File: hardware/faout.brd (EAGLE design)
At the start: 100 x 80 mm, 150 parts, among them IC2 MT48LC8M16A2, Q1 12MHz, Q4 ASFL, U1 93LC46BT-I/OT, U10 REF102AU, U11 OPA4277UA, U12 DAC8812, U13 OPA4277UA, U14 REF102AU, U15 DAC8812, U16 OPA4277UA, U17 OPA2277UA/2K5E4, U2 REF102AU, U3 L7812ACV, U4 L7912ACV, U5 LM3671MF-3.3, U6 LM3671MF-1.2, U7 M25PE16SO8N, U8 6SLX9TQG144, U9 DAC8812

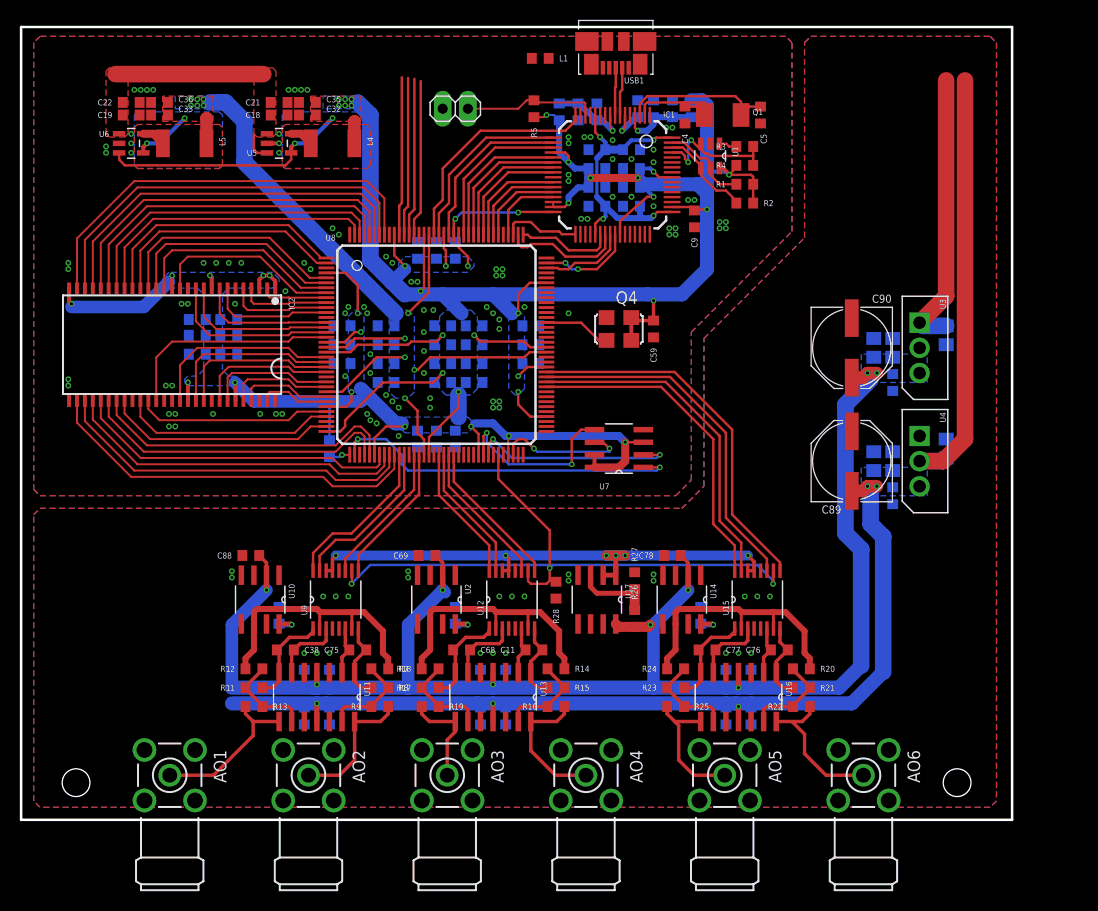
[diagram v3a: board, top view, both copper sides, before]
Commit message: WIP: Compress FAOUT-6 layout to 7cm, use space for connectors.
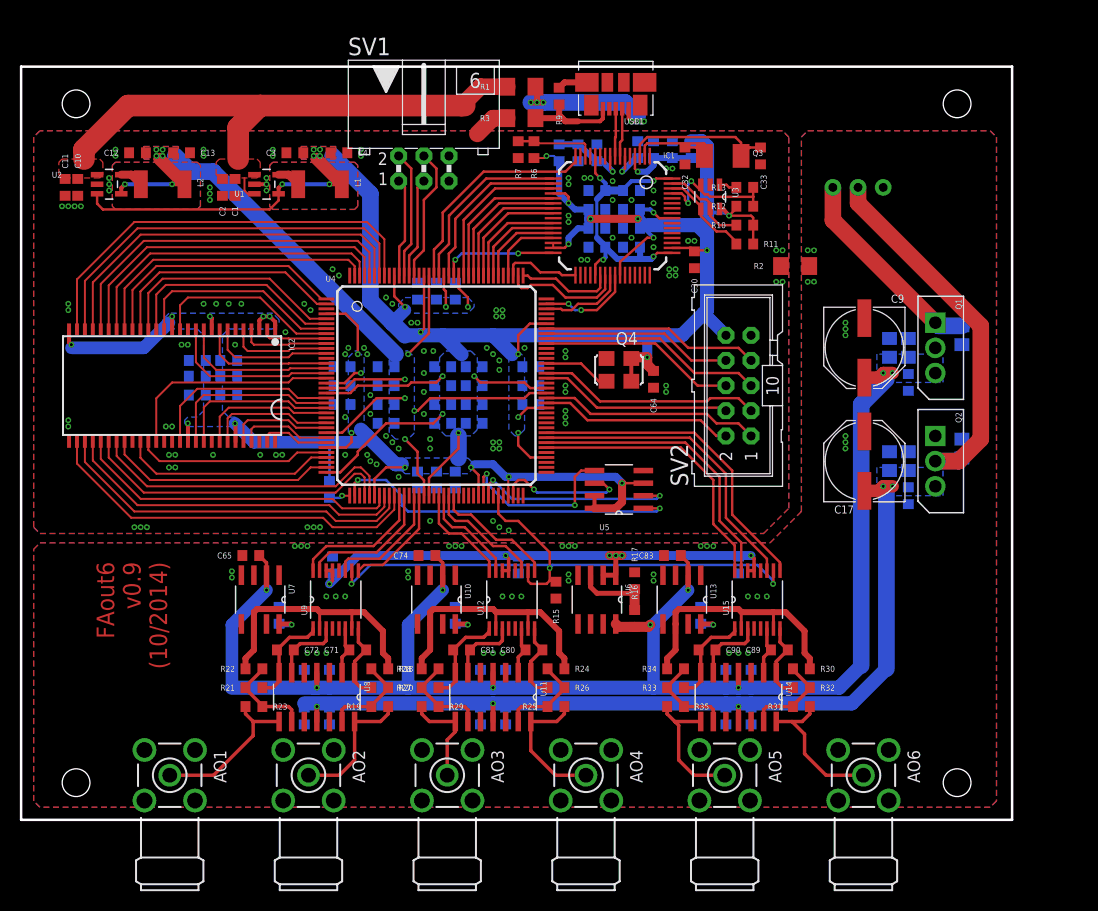
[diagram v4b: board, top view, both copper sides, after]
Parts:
- removed L3: (no value), faout:R0603
- removed L4, L5: 2.2uH, rcl:L5038P
- removed U16: OPA4277UA, faout:SOIC127P600X175-14N
- removed U17: OPA2277UA/2K5E4, faout:SOIC127P600X175-8N
- removed USB_RST: (no value), pinhead:1X02
- added C86: 1uF, faout:R0603
- added C87, C91: 100nF, faout:R0603
- added P1: TE_CONN_MTE_HEADER3R, faout:TE_CONN_MTE_HEADER3_R
- added Q2: L7912ACV, faout:TO254P450X1020X1935-3P
- added Q3: 12MHz, faout:TXC_QUARTZ_7A
- added R29, R30, R31, R34, R35: 10k, faout:R0603
- added R32, R33: 5k, faout:R0603
- added SV1: (no value), con-ml:ML6L
- added SV2: (no value), con-ml:ML10
- C1, C12, C13, C2: value 10uF -> 4.7uF; device faout:R0805 -> faout:R0603
- C11: value 20pF -> 4.7uF
- C14: value 10uF -> 100nF; device faout:R0805 -> faout:R0603
- C16, C7: value 100nF -> 10uF; device faout:R0603 -> faout:R0805
- C17, C9: value 100nF -> 100uF; device faout:R0603 -> rcl:PANASONIC_E
- C18, C8: value 4.7uF -> 10uF; device faout:R0603 -> faout:R0805
- C20: value 100nF -> 4.7uF
- C21, C22: value 4.7uF -> 100nF
- C29, C30: value 470nF -> 100nF
- C3: value 3.3uF -> 4.7uF
- C31: value 4.7uF -> 3.3uF
- C32, C33: value 4.7uF -> 18pF
- C34, C35, C43, C44, C46, C49, C56: value 4.7uF -> 470nF
- C37, C59: value 10nF -> 4.7uF
- C38: value 20pF -> 10nF
- C4: value 18pF -> 4.7uF
- C42, C48, C54, C60, C62: value 470nF -> 4.7uF
- C5: value 18pF -> 10uF; device faout:R0603 -> faout:R0805
- C64: value 4.7uF -> 10nF
- C68, C75, C76, C77: value 20pF -> 1uF
- C69, C70, C73, C78, C79, C88: value 1uF -> 100nF
- C71, C72, C80, C81: value 100nF -> 20pF
- C83: value 100nF -> 1uF
- C89, C90: value 100uF -> 20pF; device rcl:PANASONIC_E -> faout:R0603
- L1, L2: value (none) -> 2.2uH; device faout:R0603 -> rcl:L5038P
- Q1: value 12MHz -> L7812ACV; device faout:TXC_QUARTZ_7A -> faout:TO254P450X1020X1935-3P
- R1, R2: value 10k -> ferrite; device faout:R0603 -> faout:R1206
- R10: value 4.7k -> 10k
- R11, R15, R23: value 5k -> 10k
- R13: value 10k -> 2.2k
- R14: value 10k -> 4.7k
- R16: value 10k -> 13.181k
- R20: value 10k -> 5k
- R26: value 13.181k -> 5k
- R3: value 2.2k -> ferrite; device faout:R0603 -> faout:R1206
- R4, R5: value 10k -> ferrite
- R6: value 12k -> 10k
- R7: value 10k -> NC
- R8: value 5k -> 12k
- R9: value 10k -> (none)
- U1: value 93LC46BT-I/OT -> LM3671MF-3.3; device faout:SOT95P280X145-6N -> faout:SOT95P284X122-5N
- U13: value OPA4277UA -> REF102AU; device faout:SOIC127P600X175-14N -> faout:SOIC127P600X175-8N
- U14: value REF102AU -> OPA4277UA; device faout:SOIC127P600X175-8N -> faout:SOIC127P600X175-14N
- U2: value REF102AU -> LM3671MF-1.2; device faout:SOIC127P600X175-8N -> faout:SOT95P284X122-5N
- U3: value L7812ACV -> 93LC46BT-I/OT; device faout:TO254P450X1020X1935-3P -> faout:SOT95P280X145-6N
- U4: value L7912ACV -> 6SLX9TQG144; device faout:TO254P450X1020X1935-3P -> faout:TQ144
- U5: value LM3671MF-3.3 -> M25PE16SO8N; device faout:SOT95P284X122-5N -> faout:SOIC127P600X175-8N
- U6: value LM3671MF-1.2 -> OPA2277UA/2K5E4; device faout:SOT95P284X122-5N -> faout:SOIC127P600X175-8N
- U7: value M25PE16SO8N -> REF102AU
- U8: value 6SLX9TQG144 -> OPA4277UA; device faout:TQ144 -> faout:SOIC127P600X175-14N
- moved C12 78.7 mm to (11.7, 67.3), flipped to the top, turned to 180 degrees
- moved C13 78.2 mm to (16.2, 67.3), flipped to the top, turned to 0 degrees
- moved C2 77.6 mm to (20.3, 63.8), flipped to the top, turned to 270 degrees
- moved C18 76.7 mm to (94.9, 37.5), flipped to the bottom, turned to 90 degrees
- moved C1 73.3 mm to (21.6, 63.8), flipped to the top
- moved R13 72.1 mm to (73.0, 63.8), turned to 180 degrees
- moved R12 68.1 mm to (73.0, 61.9)
- moved R11 66.8 mm to (73.0, 58.1), turned to 0 degrees
- moved C11 66.5 mm to (4.45, 63.8), turned to 270 degrees
- moved U6 65.8 mm to (58.1, 22.2), turned to 270 degrees
- moved R9 64.2 mm to (54.3, 73.0), turned to 270 degrees
- moved C33 60.8 mm to (74.6, 67.0), turned to 270 degrees
- moved R8 60.2 mm to (62.2, 67.6), flipped to the bottom, turned to 90 degrees
- moved R22 55.4 mm to (23.5, 15.2)
- moved R21 55.2 mm to (23.5, 13.3), turned to 180 degrees
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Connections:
- removed net N$16: L1.1, USB1.M6
- new net N$15: R9.1, USB1.M6
- new net P1_1: SV2.1, U4.88
- new net P1_2: SV2.2, U4.87
- new net P1_3: SV2.3, U4.93
- new net P1_4: SV2.4, U4.92
- new net P1_5: SV2.5, U4.100
- new net P1_6: SV2.6, U4.99
- new net P1_7: SV2.7, U4.102
- new net P1_8: SV2.8, U4.101
- net !DAC1_CS: now also U4.50; no longer U8.50
- net !DAC1_LDAC: now also U4.48; no longer U8.48
- net !DAC2_CS: now also U4.57; no longer U8.57
- net !DAC2_LDAC: now also U4.56; no longer U8.56
- net !DAC3_CS: now also U4.80; no longer U8.84
- net !DAC3_LDAC: now also U4.79; no longer U8.83
- net !DACX_RS: now also R15.1, U4.67; no longer R28.1, U8.67
- net !RAM_CAS: now also U4.5; no longer U8.5
- net !RAM_RAS: now also U4.2; no longer U8.2
- net !RAM_WE: now also U4.6; no longer U8.6
- net !USB_OE: now also U4.111; no longer U8.111
- net !USB_RD: now also U4.114; no longer U8.114
- net !USB_RESET: now also R6.1, R7.1; no longer R5.1, USB_RST.1
- net !USB_RXF: now also U4.116; no longer U8.116
- net !USB_TXE: now also U4.115; no longer U8.115
- net !USB_WR: now also U4.112; no longer U8.112
- net +15V: now also C5.1, P1.P$1, Q1.1; no longer C1.1, U3.1
- net -15V: now also C18.1, P1.P$2, Q2.2; no longer C2.1, U4.2
- net 1V2: now also C12.1, C13.1, C52.1, C53.1, C54.1, C55.1, L2.2, U2.4, U4.128, U4.19, U4.28, U4.52, U4.89; no longer C33.1, C36.1, C41.1, C43.1, C45.1, C46.1, L5.2, U6.4, U8.128, U8.19, U8.28, U8.52, U8.89
- net 1V8: now also C25.1, C31.1; no longer C20.1, C3.1
- net 3V3: now also C3.1, C36.1, C38.1, C4.1, C41.1, C43.1, C45.1, C46.1, L1.2, R11.2, R12.2, R14.2, R4.1, R5.1, R6.2, SV2.10, U1.4, U2.3, U3.6, U4.103, U4.122, U4.125, U4.129, U4.135, U4.18, U4.20, U4.31, U4.36, U4.4, U4.42, U4.53, U4.63, U4.69, U4.76, U4.86, U4.90, U5.3, U5.7, U5.8; no longer C25.1, C31.1, C32.1, C52.1, C53.1, C54.1, C55.1, C9.1, L2.1, L3.1, L4.2, R1.2, R2.2, R4.2, R5.2, U1.6, U5.4, U6.3, U7.3, U7.7, U7.8, U8.103, U8.122, U8.125, U8.129, U8.135, U8.18, U8.20, U8.31, U8.36, U8.4, U8.42, U8.53, U8.63, U8.69, U8.76, U8.86, U8.90
- net 5V0: now also C1.1, C10.1, C11.1, C2.1, R1.2, U1.1, U1.3, U2.1; no longer C18.1, C19.1, C21.1, C22.1, U5.1, U5.3, U6.1
- net A+12V: now also C65.1, C67.1, C7.1, C74.1, C76.1, C8.1, C83.1, C85.1, C87.1, C9.+, Q1.3, R16.1, U13.2, U14.4, U6.8, U7.2, U8.4; no longer C12.1, C14.1, C66.1, C71.1, C73.1, C80.1, C82.1, C84.1, C88.1, C90.+, R26.1, U13.4, U14.2, U16.4, U17.8, U2.2, U3.3
- net A+3V3: now also C73.1, C82.1, C91.1, U6.1, U6.2; no longer U17.1, U17.2
- net A-12V: now also C14.2, C16.2, C17.-, C68.2, C70.2, C77.2, C79.2, C86.2, C88.2, Q2.3, U14.11, U8.11; no longer C13.2, C67.2, C7.2, C72.2, C74.2, C81.2, C83.2, C85.2, C89.-, U13.11, U16.11, U4.3
- net AGND: now also C14.1, C16.1, C17.+, C18.2, C5.2, C67.2, C68.1, C7.2, C70.1, C74.2, C75.2, C76.2, C77.1, C79.1, C8.2, C83.2, C85.2, C86.1, C87.2, C88.1, C9.-, C91.2, P1.P$3, Q1.2, Q2.1, R15.2, R17.2, R2.1, U13.4, U14.10, U14.12, U14.3, U14.5, U6.4, U7.4, U8.10, U8.12, U8.3, U8.5; no longer C1.2, C12.2, C13.1, C14.2, C2.2, C67.1, C7.1, C70.2, C71.2, C72.1, C74.1, C79.2, C80.2, C81.1, C83.1, C85.1, C88.2, C89.+, C90.-, R27.2, R28.2, U13.10, U13.12, U13.3, U13.5, U14.4, U16.10, U16.12, U16.3, U16.5, U17.4, U2.4, U3.2, U4.1
- net CLK_IN: now also U4.95; no longer U8.95
- net DAC1_CLK: now also U4.47; no longer U8.47
- net DAC1_IOUTA: now also C72.2, U8.6; no longer C38.2, U11.6
- net DAC1_IOUTB: now also C71.2, U8.2; no longer C75.2, U11.2
- net DAC1_RFBA: now also C72.1, R21.1, U8.7; no longer C38.1, R11.1, U11.7
- net DAC1_RFBB: now also C71.1, R20.1, U8.1; no longer C75.1, R8.1, U11.1
- net DAC1_SDI: now also U4.51; no longer U8.51
- net DAC1_VOUTA: now also R23.1, U8.8; no longer R13.1, U11.8
- net DAC1_VOUTB: now also R19.1, U8.14; no longer R9.1, U11.14
- net DAC1_VREF: now also R18.2, R22.2, U7.6; no longer R12.2, R7.2, U10.6
- net DAC2_CLK: now also U4.55; no longer U8.55
- net DAC2_IOUTA: now also C81.2, U11.6; no longer C68.2, U13.6
- net DAC2_IOUTB: now also C80.2, U11.2; no longer C11.2, U13.2
- net DAC2_RFBA: now also C81.1, R27.1, U11.7; no longer C68.1, R17.1, U13.7
- net DAC2_RFBB: now also C80.1, R26.1, U11.1; no longer C11.1, R15.1, U13.1
- net DAC2_SDI: now also U4.58; no longer U8.58
- net DAC2_VOUTA: now also R29.1, U11.8; no longer R19.1, U13.8
- net DAC2_VOUTB: now also R25.1, U11.14; no longer R16.1, U13.14
- net DAC2_VREF: now also R24.2, R28.2, U10.6; no longer R14.2, R18.2, U2.6
- net DAC3_CLK: now also U4.78; no longer U8.82
- net DAC3_IOUTA: now also C90.2, U14.6; no longer C77.2, U16.6
- net DAC3_IOUTB: now also C89.2, U14.2; no longer C76.2, U16.2
- net DAC3_RFBA: now also C90.1, R33.1, U14.7; no longer C77.1, R23.1, U16.7
- net DAC3_RFBB: now also C89.1, R32.1, U14.1; no longer C76.1, R21.1, U16.1
- net DAC3_SDI: now also U4.81; no longer U8.85
- net DAC3_VOUTA: now also R35.1, U14.8; no longer R25.1, U16.8
- net DAC3_VOUTB: now also R31.1, U14.14; no longer R22.1, U16.14
- net DAC3_VREF: now also R30.2, R34.2, U13.6; no longer R20.2, R24.2, U14.6
- net EECS: now also R10.1, U3.5; no longer R1.1, U1.5
- net EEDATA: now also R12.1, R13.1, U3.3; no longer R3.1, R4.1, U1.3
- net EESK: now also R11.1, U3.4; no longer R2.1, U1.4
- net FLASH_CS: now also U4.38, U5.1; no longer U7.1, U8.38
- net FLASH_MISO: now also U4.65, U5.2; no longer U7.2, U8.65
- net FLASH_MOSI: now also U4.64, U5.5; no longer U7.5, U8.64
- net FLASH_SCK: now also U4.70, U5.6; no longer U7.6, U8.70
- net GND: now also C1.2, C11.2, C12.2, C13.2, C2.2, C38.2, R2.2, R3.2, R7.2, R8.2, SV1.5, SV1.6, SV2.9, U2.2, U3.2, U4.104, U4.105, U4.108, U4.113, U4.13, U4.130, U4.136, U4.144, U4.25, U4.3, U4.34, U4.49, U4.54, U4.59, U4.60, U4.61, U4.62, U4.66, U4.68, U4.73, U4.77, U4.82, U4.83, U4.84, U4.85, U4.91, U4.94, U4.96, U4.97, U4.98, U5.4; no longer C16.2, C17.2, C18.2, C5.2, C8.2, C9.2, L1.2, R6.2, U5.2, U6.2, U7.4, U8.108, U8.113, U8.13, U8.130, U8.136, U8.144, U8.25, U8.3, U8.49, U8.54, U8.60, U8.68, U8.73, U8.77, U8.91, U8.96, USB_RST.2
- net GPIO_0_0: now also SV1.1, U4.134; no longer U8.134
- net GPIO_0_1: now also SV1.2, U4.133; no longer U8.133
- net GPIO_0_2: now also SV1.3, U4.132; no longer U8.132
- net GPIO_0_3: now also SV1.4, U4.131; no longer U8.131
- net N$1: now also C32.1, Q3.1; no longer C4.1, Q1.1
- net N$10: now also R30.1, R31.2, R32.2, U14.13; no longer R20.1, R21.2, R22.2, U16.13
- net N$11: now also C75.1, U10.8; no longer C70.1, U2.8
- net N$12: now also C84.1, U13.8; no longer C79.1, U14.8
- net N$13: now also R16.2, R17.1, U6.3; no longer R26.2, R27.1, U17.3
- net N$14: now also R33.2, R34.1, R35.2, U14.9; no longer R23.2, R24.1, R25.2, U16.9
- net N$2: now also C33.1, Q3.2; no longer C5.1, Q1.2
- net N$20: now also R27.2, R28.1, R29.2, U11.9; no longer R17.2, R18.1, R19.2, U13.9
- net N$21: now also R24.1, R25.2, R26.2, U11.13; no longer R14.1, R15.2, R16.2, U13.13
- net N$24: now also L1.1, U1.5; no longer L4.1, U5.5
- net N$25: now also L2.1, U2.5; no longer L5.1, U6.5
- net N$4: now also C66.1, U7.8; no longer C65.1, U10.8
- net N$5: now also C19.1, C21.1, R5.2; no longer C16.1, C8.1, L3.2
- net N$6: now also R13.2, U3.1; no longer R3.2, U1.1
- net N$7: now also C20.1, C22.1, R4.2; no longer C10.1, C17.1, L2.2
- net N$8: now also R21.2, R22.1, R23.2, U8.9; no longer R11.2, R12.1, R13.2, U11.9
- net N$9: now also R18.1, R19.2, R20.2, U8.13; no longer R7.1, R8.2, R9.2, U11.13
- net RAM_A0: now also U4.140; no longer U8.140
- net RAM_A1: now also U4.139; no longer U8.139
- net RAM_A10: now also U4.141; no longer U8.141
- net RAM_A11: now also U4.35; no longer U8.35
- net RAM_A2: now also U4.138; no longer U8.138
- net RAM_A3: now also U4.137; no longer U8.137
- net RAM_A4: now also U4.46; no longer U8.46
- net RAM_A5: now also U4.45; no longer U8.45
- net RAM_A6: now also U4.44; no longer U8.44
- net RAM_A7: now also U4.43; no longer U8.43
- net RAM_A8: now also U4.40; no longer U8.40
- net RAM_A9: now also U4.41; no longer U8.41
- net RAM_BA0: now also U4.143; no longer U8.143
- net RAM_BA1: now also U4.142; no longer U8.142
- net RAM_CKE: now also U4.33; no longer U8.33
- net RAM_CLK: now also U4.32; no longer U8.32
- net RAM_CS: now also U4.1; no longer U8.1
- net RAM_DQ0: now also U4.9; no longer U8.9
- net RAM_DQ1: now also U4.10; no longer U8.10
- net RAM_DQ10: now also U4.23; no longer U8.23
- net RAM_DQ11: now also U4.24; no longer U8.24
- net RAM_DQ12: now also U4.26; no longer U8.26
- net RAM_DQ13: now also U4.27; no longer U8.27
- net RAM_DQ14: now also U4.29; no longer U8.29
- net RAM_DQ15: now also U4.30; no longer U8.30
- net RAM_DQ2: now also U4.11; no longer U8.11
- net RAM_DQ3: now also U4.12; no longer U8.12
- net RAM_DQ4: now also U4.14; no longer U8.14
- net RAM_DQ5: now also U4.15; no longer U8.15
- net RAM_DQ6: now also U4.16; no longer U8.16
- net RAM_DQ7: now also U4.8; no longer U8.8
- net RAM_DQ8: now also U4.21; no longer U8.21
- net RAM_DQ9: now also U4.22; no longer U8.22
- net RAM_DQMH: now also U4.17; no longer U8.17
- net RAM_DQML: now also U4.7; no longer U8.7
- net RESET: now also R14.1, U4.37; no longer R10.1, U8.37
- net TCK: now also U4.109; no longer U8.109
- net TDI: now also U4.110; no longer U8.110
- net TDO: now also U4.106; no longer U8.106
- net TMS: now also U4.107; no longer U8.107
- net USB_CLKOUT: now also U4.123; no longer U8.123
- net USB_D0: now also U4.127; no longer U8.127
- net USB_D1: now also U4.126; no longer U8.126
- net USB_D2: now also U4.124; no longer U8.124
- net USB_D3: now also U4.121; no longer U8.121
- net USB_D4: now also U4.120; no longer U8.120
- net USB_D5: now also U4.119; no longer U8.119
- net USB_D6: now also U4.118; no longer U8.118
- net USB_D7: now also U4.117; no longer U8.117
- net USB_GND: now also R3.1, R9.2
- net USB_REF: now also R8.1; no longer R6.1
- net USB_V: now also R1.1
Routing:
- net 5V0: track 18.0 -> 55.3 mm
- net P1_5: track 0.00 -> 22.6 mm
- net P1_3: track 0.00 -> 22.5 mm
- net P1_1: track 0.00 -> 22.2 mm
- net P1_7: track 0.00 -> 22.0 mm
- net P1_6: track 0.00 -> 19.9 mm
- net P1_2: track 0.00 -> 19.5 mm
- net P1_4: track 0.00 -> 19.5 mm
- net P1_8: track 0.00 -> 19.2 mm
- net USB_V: track 0.00 -> 18.8 mm, vias 0 -> 6
- net USB_GND: track 0.00 -> 9.54 mm
- net +15V: track 28.4 -> 20.7 mm
- net 3V3: track 344.1 -> 351.2 mm, vias 43 -> 41
- net GPIO_0_0: track 16.0 -> 10.0 mm
- net GPIO_0_2: track 15.9 -> 10.2 mm
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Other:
- board size 100 x 80 mm -> 100 x 76 mm
- board text added: "FAout6 v0.9 (10/2014)"

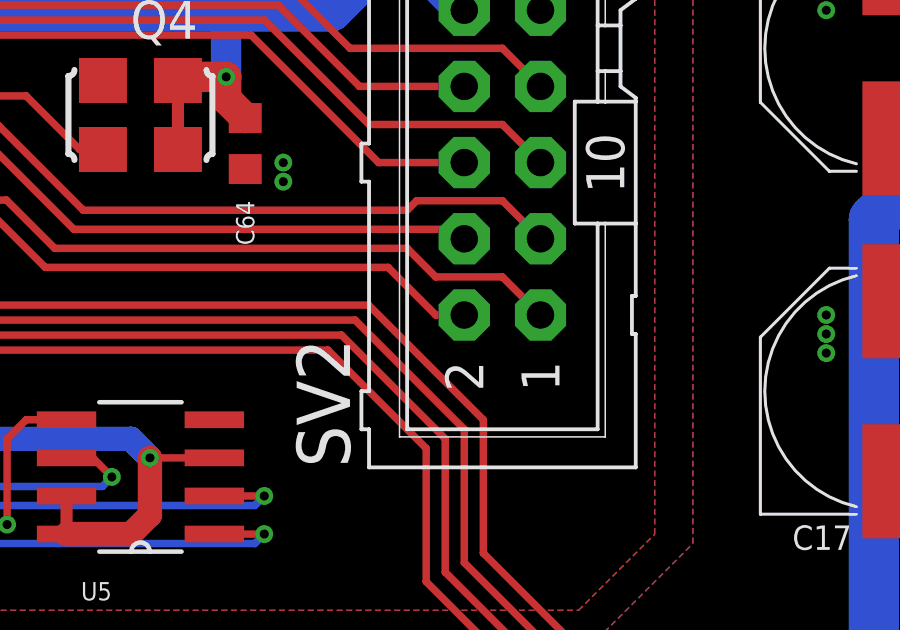
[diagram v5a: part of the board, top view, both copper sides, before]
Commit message: Update UCF file for new board layout.
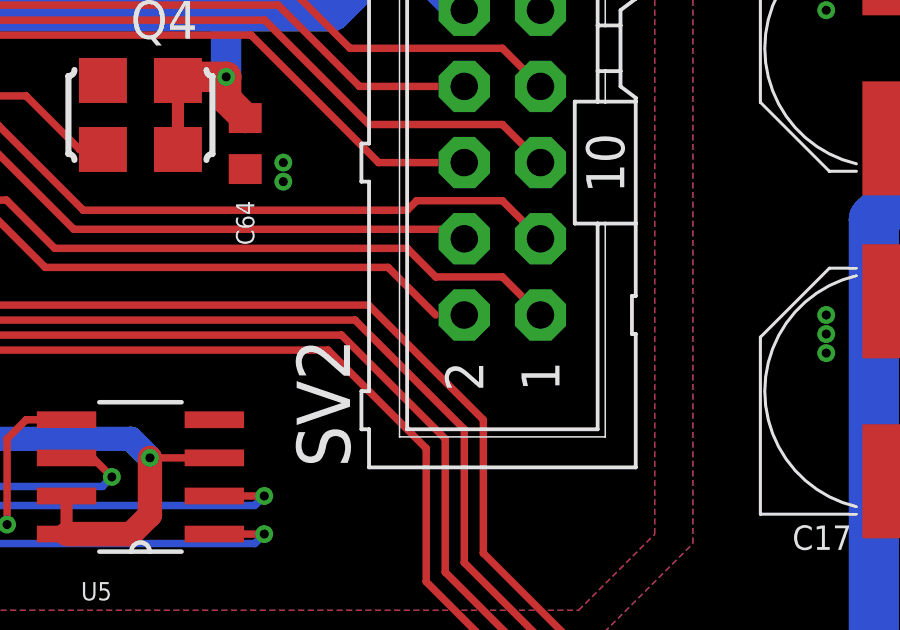
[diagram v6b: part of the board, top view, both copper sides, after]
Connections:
- removed net P1_8: SV2.8, U4.101
- new net P1_0: SV2.1, U4.88
- net P1_1: now also SV2.2, U4.87; no longer SV2.1, U4.88
- net P1_2: now also SV2.3, U4.93; no longer SV2.2, U4.87
- net P1_3: now also SV2.4, U4.92; no longer SV2.3, U4.93
- net P1_4: now also SV2.5, U4.100; no longer SV2.4, U4.92
- net P1_5: now also SV2.6, U4.99; no longer SV2.5, U4.100
- net P1_6: now also SV2.7, U4.102; no longer SV2.6, U4.99
- net P1_7: now also SV2.8, U4.101; no longer SV2.7, U4.102
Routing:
- net P1_0: track 0.00 -> 22.2 mm
- net P1_8: track 19.2 -> 0.00 mm
- net P1_1: track 22.2 -> 18.5 mm
- net P1_4: track 19.5 -> 22.6 mm
- net P1_3: track 22.5 -> 19.5 mm
- net P1_2: track 19.5 -> 22.5 mm
- net P1_5: track 22.6 -> 19.9 mm
- net P1_7: track 22.0 -> 19.2 mm
- net P1_6: track 19.9 -> 22.0 mm
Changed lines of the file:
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@@
 <wire x1="54.8325" y1="74.415" x2="54.2925" y2="73.875" width="0.6096" layer="1"/>
 </signal>
-<signal name="P1_2">
-<contactref element="U4" pad="87"/>
-<contactref element="SV2" pad="2"/>
-<wire x1="53.01" y1="42.065" x2="55.4075" y2="42.065" width="0.25" layer="1"/>
-<wire x1="55.4075" y1="42.065" x2="57.15" y2="40.3225" width="0.25" layer="1"/>
-<wire x1="57.15" y1="40.3225" x2="68.58" y2="40.3225" width="0.25" layer="1"/>
-<wire x1="68.58" y1="40.3225" x2="70.1675" y2="38.735" width="0.25" layer="1"/>
-<wire x1="70.1675" y1="38.735" x2="71.12" y2="38.735" width="0.25" layer="1"/>
-</signal>
-<signal name="P1_1">
+<signal name="P1_0">
 <contactref element="U4" pad="88"/>
 <contactref element="SV2" pad="1"/>
@@
 <wire x1="72.39" y1="40.005" x2="73.66" y2="38.735" width="0.25" layer="1"/>
 </signal>
-<signal name="P1_4">
+<signal name="P1_3">
 <contactref element="U4" pad="92"/>
 <contactref element="SV2" pad="4"/>
@@
 <wire x1="70.8025" y1="41.5925" x2="71.12" y2="41.275" width="0.25" layer="1"/>
 </signal>
-<signal name="P1_3">
+<signal name="P1_2">
 <contactref element="U4" pad="93"/>
 <contactref element="SV2" pad="3"/>
@@
 <wire x1="72.39" y1="42.545" x2="73.66" y2="41.275" width="0.25" layer="1"/>
 </signal>
-<signal name="P1_7">
+<signal name="P1_6">
 <contactref element="U4" pad="102"/>
 <contactref element="SV2" pad="7"/>
@@
 <wire x1="72.39" y1="47.625" x2="73.66" y2="46.355" width="0.25" layer="1"/>
 </signal>
-<signal name="P1_8">
+<signal name="P1_7">
 <contactref element="U4" pad="101"/>
 <contactref element="SV2" pad="8"/>
@@
 <wire x1="67.6275" y1="46.355" x2="71.12" y2="46.355" width="0.25" layer="1"/>
 </signal>
-<signal name="P1_5">
+<signal name="P1_4">
 <contactref element="U4" pad="100"/>
 <contactref element="SV2" pad="5"/>
@@
 <wire x1="72.39" y1="45.085" x2="73.66" y2="43.815" width="0.25" layer="1"/>
 </signal>
-<signal name="P1_6">
+<signal name="P1_5">
 <contactref element="U4" pad="99"/>
 <contactref element="SV2" pad="6"/>
@@
 <wire x1="68.2625" y1="43.815" x2="71.12" y2="43.815" width="0.25" layer="1"/>
 </signal>
+<signal name="P1_1">
+<contactref element="SV2" pad="2"/>
+<contactref element="U4" pad="87"/>
+<wire x1="53.01" y1="42.065" x2="55.4075" y2="42.065" width="0.25" layer="1"/>
+<wire x1="55.4075" y1="42.065" x2="57.15" y2="40.3225" width="0.25" layer="1"/>
+<wire x1="57.15" y1="40.3225" x2="68.58" y2="40.3225" width="0.25" layer="1"/>
+<wire x1="68.58" y1="40.3225" x2="70.1675" y2="38.735" width="0.25" layer="1"/>
+<wire x1="70.1675" y1="38.735" x2="71.12" y2="38.735" width="0" layer="19" extent="1-1"/>
+</signal>
 </signals>
